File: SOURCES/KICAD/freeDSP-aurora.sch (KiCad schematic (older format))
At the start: 71 parts, among them IC101 IC_ADAU1452, IC102 IC_25AA1024, IC103 IC_TLE2426ID, IC104 IC_ADM811TARTZ, IC105 IC_LM1117MP-5.0, IC106 IC_NCP1117LPST33, IC107 IC_LM1117MP-5.0, Q101 Q_STD2805, X101 MicroMatch14, X102 HDR_02x08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

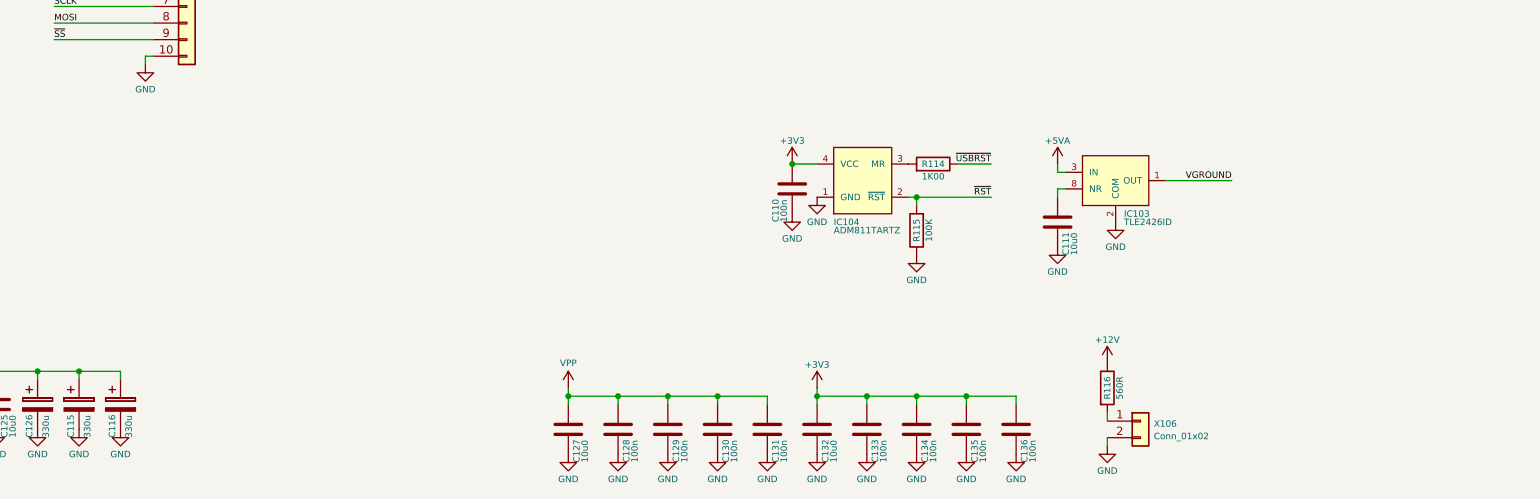
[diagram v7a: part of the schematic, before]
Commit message: Added extra caps on analog supply rail
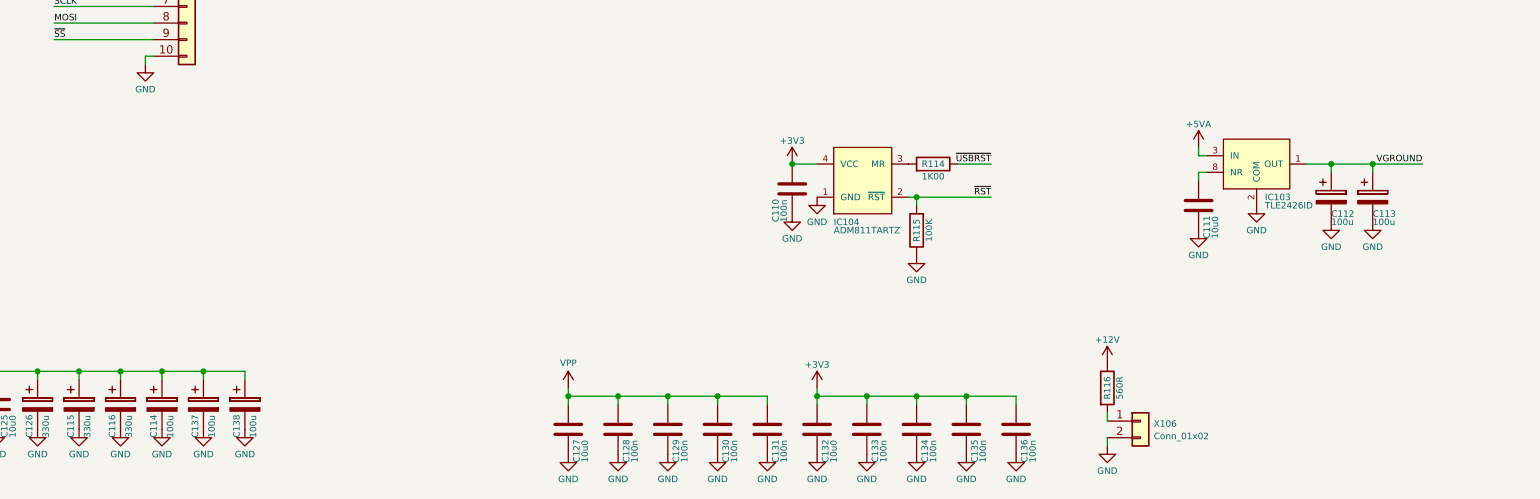
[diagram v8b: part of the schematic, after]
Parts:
- added C112, C113, C114, C137, C138: CAP_100u_20%_25V_ALUM_RADIAL, rklib:RD2_D5_L11, symbol freeDSP-aurora-rescue:CAP_100u_20%_25V_ALUM_RADIAL
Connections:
- net +5VA: now also C114.1, C137.1, C138.1
- net GND: now also C112.2, C113.2, C114.2, C137.2, C138.2
- net VGROUND: now also C112.1, C113.1
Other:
- moved on the sheet: C111, IC103
